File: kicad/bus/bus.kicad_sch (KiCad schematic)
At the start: 24 parts

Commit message: Finished schematic for motherboard
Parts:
- added J1: Barrel_Jack, Connector_BarrelJack:BarrelJack_Horizontal, symbol Connector:Barrel_Jack
- added R10, R13: 1k, Resistor_THT:R_Axial_DIN0207_L6.3mm_D2.5mm_P7.62mm_Horizontal, symbol Device:R
- added U14, U28, U31: ~, Package_DIP:DIP-14_W7.62mm, symbol custom_symbol_lib:dual_latch
- added U15: ~, Package_DIP:DIP-20_W7.62mm, symbol custom_symbol_lib:rising_edge_8_bit_latch
- added U16, U30: ~, Package_DIP:DIP-14_W7.62mm, symbol custom_symbol_lib:quad_and
- added U17, U18, U19, U20, U21, U22, U26, U27: ~, custom_footprint_library:jumper, symbol custom_symbol_lib:jumper
- added U23: ~, Package_DIP:DIP-14_W7.62mm, symbol custom_symbol_lib:6xNOT
- added U24: ~, Connector_PinHeader_2.54mm:PinHeader_1x22_P2.54mm_Vertical, symbol custom_symbol_lib:bus_edge_connector
- added U25: ~, Package_DIP:DIP-14_W7.62mm, symbol custom_symbol_lib:dual_4_input_OR
- added U29: L7805, Package_TO_SOT_THT:TO-220-3_Vertical, symbol Regulator_Linear:L7805
- R1, R11, R12, R2, R3, R4, R5, R6, R7, R8, R9: value R -> 1k; footprint (none) -> Resistor_THT:R_Axial_DIN0207_L6.3mm_D2.5mm_P7.62mm_Horizontal
- U1, U10, U11, U12, U13, U2, U3, U4, U5, U6, U7, U8, U9: value (none) -> ~
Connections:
- net at R11.2, R2.1, R4.1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: now also R1.2, R12.1, R3.2, R7.2, R8.1, U9.12 (3A), U9.13 (3B), J1.2, R10.1, R13.1, U14.10 (1RESET), U14.4 (0RESET), U14.6 (0SET), U14.7 (GND), U14.8 (1SET), U15.10 (GND), U16.4 (2A), U16.5 (2B), U16.7 (GND), U17.2 (GND), U18.2 (GND), U19.2 (GND), U20.2 (GND), U21.2 (GND), U22.2 (GND), U23.11 (I4), U23.13 (I5), U23.7 (GND), U24.13 (GND), U25.12 (B3), U25.7 (GND), U26.2 (GND), U27.2 (GND), U28.10 (1RESET), U28.4 (0RESET), U28.6 (0SET), U28.7 (GND), U28.8 (1SET), U29.2 (GND), U30.4 (2A), U30.5 (2B), U30.7 (GND), U31.10 (1RESET), U31.4 (0RESET), U31.6 (0SET), U31.7 (GND), U31.8 (1SET); no longer R1.1, R12.2, R3.1, R7.1, R8.2, U8.10 (B1), U8.11 (B2)
- net at R2.2: now also U6.9 (READ_READY), U25.3 (A1); no longer U4.9 (READ_READY)
- net at U3.9 (READ_READY): now also R8.2, U25.9 (B0); no longer R5.2
- net at U2.10 (CLK_A), U3.10 (CLK_A), U4.10 (CLK_A)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: now also U14.11 (1CLK), U14.3 (0CLK), U24.10 (CLK_A), U30.10 (4A), U30.12 (3B), U31.11 (1CLK)
- net at U2.11 (CLK_B), U3.11 (CLK_B), U4.11 (CLK_B)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: now also U24.11 (CLK_B), U28.11 (1CLK), U28.3 (0CLK)
- net at U10.16 (V+), U10.6 (E1), U11.16 (V+)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: now also U8.14 (V+), U9.14 (V+), U14.14 (V+), U15.20 (V+), U16.14 (V+), U23.14 (V+), U24.12 (V+), U25.14 (V+), U28.14 (V+), U29.3 (OUT), U30.14 (V+), U31.14 (V+)
- net at U2.14 (D0), U3.14 (D0), U4.14 (D0)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: now also U15.19 (Q0), U15.2 (D0), U24.14 (D0)
- net at U2.15 (D1), U3.15 (D1), U4.15 (D1)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: now also U15.18 (Q1), U15.3 (D1), U24.15 (D1)
- net at U2.16 (D2), U3.16 (D2), U4.16 (D2)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: now also U15.17 (Q2), U15.4 (D2), U24.16 (D2)
- net at U2.17 (D3), U3.17 (D3), U4.17 (D3)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: now also U15.16 (Q3), U15.5 (D3), U24.17 (D3)
- net at U2.18 (D4), U3.18 (D4), U4.18 (D4)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: now also U15.15 (Q4), U15.6 (D4), U24.18 (D4)
- net at U2.19 (D5), U3.19 (D5), U4.19 (D5)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: now also U15.14 (Q5), U15.7 (D5), U24.19 (D5)
- net at U2.20 (D6), U3.20 (D6), U4.20 (D6)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: now also U15.13 (Q6), U15.8 (D6), U24.20 (D6)
- net at U2.21 (D7), U3.21 (D7), U4.21 (D7)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: now also U15.12 (Q7), U15.9 (D7), U24.21 (D7)
- net at U2.22 (FAULT), U8.9 (B0): now also R11.1; no longer R7.2
- net at U2.9 (READ_READY): now also R10.2, U25.10 (B1); no longer R6.2
- net at U3.22 (FAULT), U8.5 (A3): now also R9.1; no longer R8.1
- net at U6.22 (FAULT), U8.3 (A1): now also R3.1; no longer R11.1
- net at U7.22 (FAULT), U8.2 (A0): now also R1.1; no longer R12.1
- net at R4.2, U7.9 (READ_READY): now also U25.2 (A0)
- net at U5.9 (READ_READY): now also R5.2, U25.4 (A2); no longer R1.2
- net at U12.4 (E2#), U13.4 (E2#): now also U23.6 (O2)
- net at U10.4 (E2#), U11.4 (E2#): now also U23.4 (O1)
- net at U9.10 (Q2): now also U31.3 (0CLK)
- net at U9.4 (Q1): now also U26.1 (IN)
- net at U9.5 (1A): now also U25.13 (OA)
- net at U9.6 (1B): now also U25.1 (OB)
- net at U9.8 (2A): now also U30.8 (4Q)
- net at U9.9 (2B): now also U14.13 (1Q), U28.9 (1D)
- net at U1.1 (Move): now also U27.1 (IN)
- net at U1.2 (Done): now also U22.3 (OUT)
- net at U4.22 (FAULT), U8.4 (A2): now also R7.1; no longer R9.1
- new net: U18.1 (IN), U30.11 (3Q)
- new net: U15.11 (CLK), U18.3 (OUT)
- new net: U19.1 (IN), U21.1 (IN), U28.13 (1Q), U31.9 (1D)
- new net: U16.1 (1A), U16.13 (3A), U19.3 (OUT)
- new net: U16.3 (1Q), U17.1 (IN), U23.9 (I3)
- new net: U17.3 (OUT), U8.10 (B1)
- new net: R12.2, U24.22 (FAULT), U8.11 (B2)
- new net: U20.1 (IN), U31.1 (0Q)
- new net: U16.10 (4A), U16.2 (1B), U20.3 (OUT)
- new net: R13.2, U24.9 (READ_READY), U25.11 (B2)
- new net: R6.2, U25.5 (A3), U4.9 (READ_READY)
- new net: U27.3 (OUT), U30.1 (1A), U30.9 (4B)
- new net: U14.5 (0D), U26.3 (OUT), U30.13 (3A)
- new net: U28.2 (0Q#), U30.2 (1B)
- new net: U30.3 (1Q), U31.5 (0D)
- new net: U14.9 (1D), U28.1 (0Q)
- new net: U14.1 (0Q), U28.5 (0D)
- new net: U15.1 (OE#), U23.2 (O0)
- new net: U21.3 (OUT), U23.5 (I2)
- new net: U16.11 (3Q), U23.1 (I0)
- new net: U16.12 (3B), U16.9 (4B), U23.8 (03)
- new net: U16.8 (4Q), U23.3 (I1)
- new net: U22.1 (IN), U31.13 (1Q)
- new net: J1.1, U29.1 (IN)
- no-connect marks 32 -> 50
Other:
- note added: "Extra"
- moved on the sheet: R4, U1, U10, U11, U12, U13, U2, U3, U4, U5, U6, U7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

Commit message: stuff
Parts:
- removed R12: 1k, Resistor_THT:R_Axial_DIN0207_L6.3mm_D2.5mm_P7.62mm_Horizontal, symbol Device:R
- added R14: 1k, custom_footprint_library:0.4_pitch_resistor, symbol Device:R
- added U32, U33: ~, custom_footprint_library:jumper, symbol custom_symbol_lib:jumper
- added U34: ~, Connector_PinHeader_2.54mm:PinHeader_1x07_P2.54mm_Vertical, symbol custom_symbol_lib:bus_to_startup_ctrl
- R1, R10, R11, R13, R2, R3, R4, R5, R6, R7, R8, R9: footprint Resistor_THT:R_Axial_DIN0207_L6.3mm_D2.5mm_P7.62mm_Horizontal -> custom_footprint_library:0.4_pitch_resistor
- U1: footprint Connector_PinHeader_2.54mm:PinHeader_1x10_P2.54mm_Vertical -> Connector_PinHeader_2.54mm:PinHeader_1x11_P2.54mm_Vertical
- U2, U24, U3, U4, U5, U6, U7: footprint Connector_PinHeader_2.54mm:PinHeader_1x22_P2.54mm_Vertical -> Connector_PinHeader_2.54mm:PinHeader_1x23_P2.54mm_Vertical
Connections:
- net at J1.2, R1.2, R10.1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: now also R14.2, U32.2 (GND), U33.2 (GND), U34.2 (GND); no longer U16.4 (2A), U16.5 (2B), U30.4 (2A), U30.5 (2B)
- net at U21.1 (IN), U28.13 (1Q), U31.9 (1D): now also U30.4 (2A); no longer U19.1 (IN)
- net at U24.22 (FAULT), U8.11 (B2): now also R14.1
- net at U20.1 (IN): now also U16.6 (2Q); no longer U31.1 (0Q)
- net at U14.11 (1CLK), U14.3 (0CLK), U2.10 (CLK_A)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: now also U34.3 (A_CLK)
- net at U2.11 (CLK_B), U24.11 (CLK_B), U28.11 (1CLK)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: now also U34.4 (B_CLK)
- net at U10.16 (V+), U10.6 (E1), U11.16 (V+)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: now also U34.1 (V+)
- net at U30.6 (2Q): now also U19.1 (IN)
- net at U5.22 (FAULT), U9.3 (Q0): now also U34.7 (FAULT)
- new net: U16.5 (2B), U2.23 (ENABLE), U24.23 (ENABLE), U3.23 (ENABLE), U30.5 (2B), U32.3 (OUT), U4.23 (ENABLE), U5.23 (ENABLE), U6.23 (ENABLE), U7.23 (ENABLE)
- new net: U33.1 (IN), U34.5 (START)
- new net: U1.11 (Start), U33.3 (OUT)
- new net: U32.1 (IN), U34.6 (ENABLE)
- new net: U16.4 (2A), U31.1 (0Q)
- no-connect marks 50 -> 48
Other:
- moved on the sheet: R11, R3, R7, R9, U17, U18, U19, U20, U21, U22, U23

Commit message: Done w/ ALU schematic
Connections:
- net at U13.9 (Y6): now also U6.3 (READ_2)
- no-connect marks 48 -> 46
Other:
- note added: "14 3 2"
- note removed: "3 2"
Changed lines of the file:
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@@
 	)
 	(no_connect
-		(at 237.49 294.64)
-	)
-	(no_connect
 		(at 476.25 227.33)
 	)
@@
 	)
 	(no_connect
-		(at 313.69 224.79)
-	)
-	(no_connect
 		(at 516.89 215.9)
 	)
@@
 	(wire
 		(pts
+			(xy 311.15 224.79) (xy 313.69 224.79)
+		)
+		(stroke
+			(width 0)
+			(type default)
+		)
+	)
+	(wire
+		(pts
 			(xy 260.35 168.91) (xy 240.03 168.91)
 		)
@@
 	(wire
 		(pts
+			(xy 237.49 294.64) (xy 311.15 294.64)
+		)
+		(stroke
+			(width 0)
+			(type default)
+		)
+	)
+	(wire
+		(pts
 			(xy 170.18 129.54) (xy 170.18 134.62)
 		)
@@
 	(wire
 		(pts
+			(xy 311.15 294.64) (xy 311.15 224.79)
+		)
+		(stroke
+			(width 0)
+			(type default)
+		)
+	)
+	(wire
+		(pts
 			(xy 185.42 179.07) (xy 185.42 154.94)
 		)
@@
 		)
 	)
-	(text "3\n2"
+	(text "14\n3\n2"
 		(exclude_from_sim no)
-		(at 299.72 228.6 0)
+		(at 299.72 227.33 0)
 		(effects
 			(font

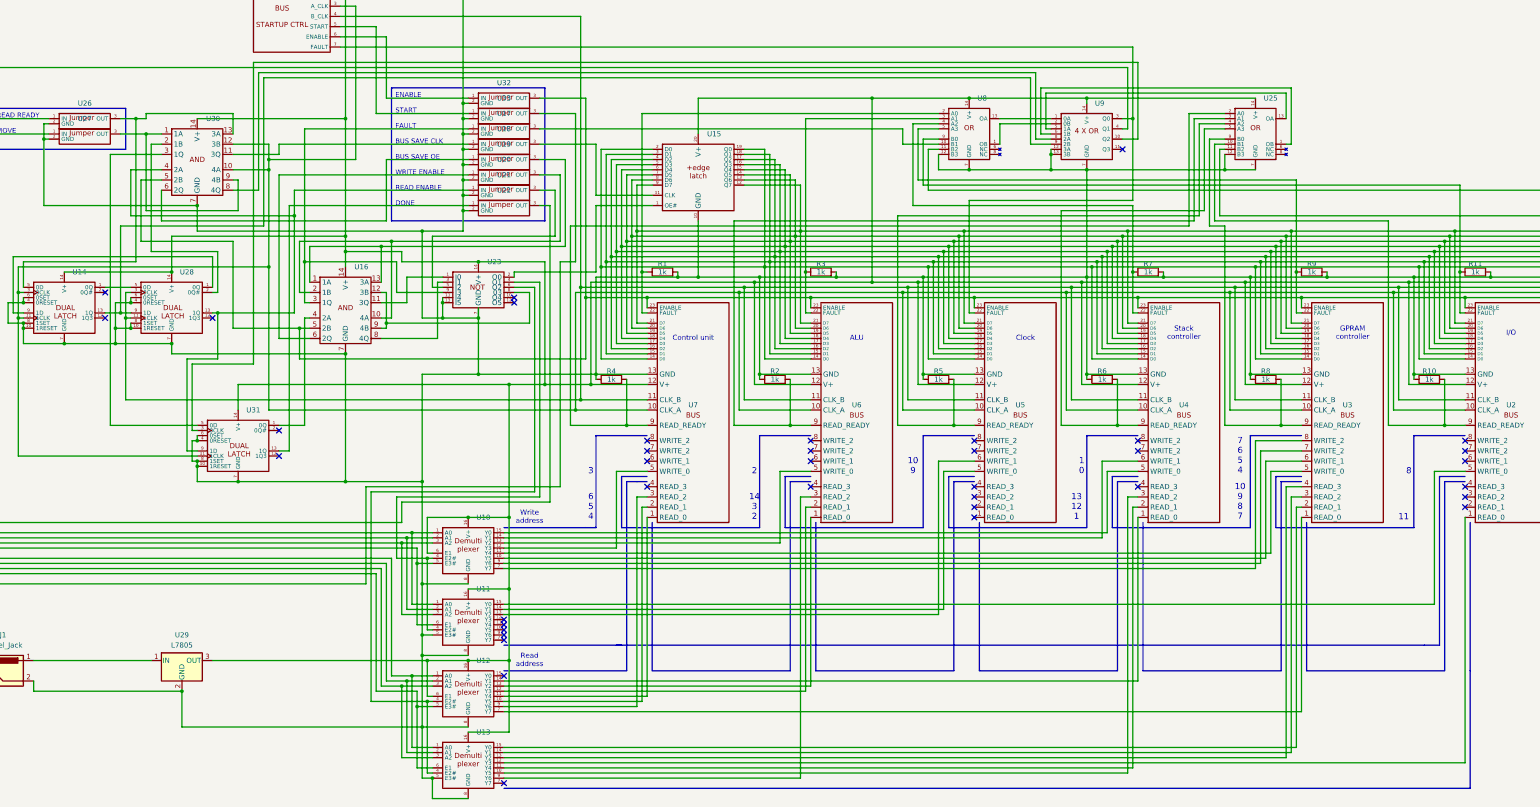
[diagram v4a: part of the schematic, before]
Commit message: Finished IO controller schematic
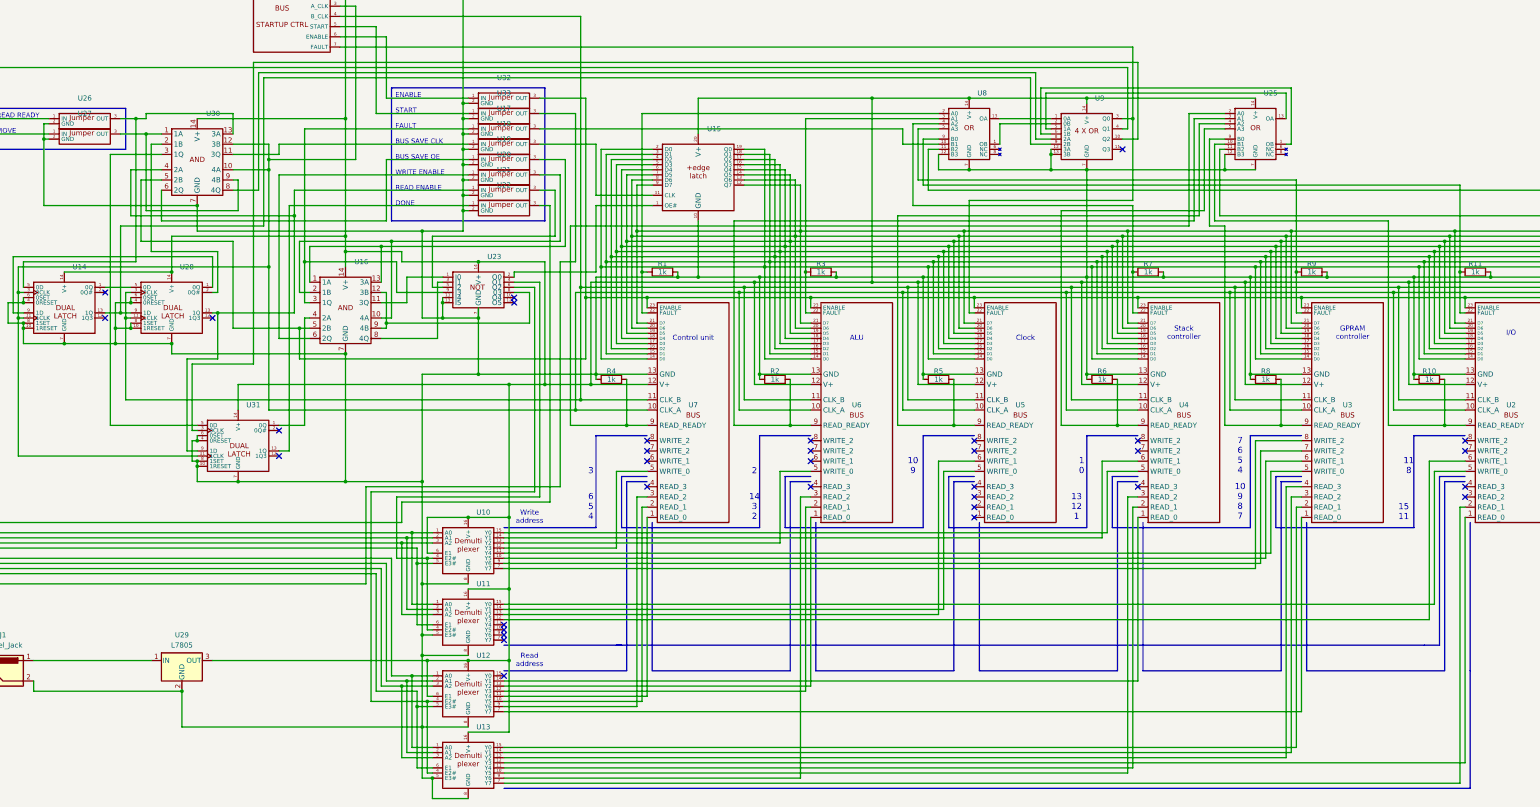
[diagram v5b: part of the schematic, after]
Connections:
- net at U2.2 (READ_1): now also U13.7 (Y7)
- net at U2.6 (WRITE_1): now also U11.12 (Y3)
- no-connect marks 46 -> 42
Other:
- note added: "11 8"
- note added: "15 11"
- note removed: "11"
- note removed: "8"
